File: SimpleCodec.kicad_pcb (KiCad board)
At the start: 4 copper layers, 59 x 95 mm, 89 parts, among them J1 RPI_ADC, J2 RP_GPIO, U1 AMS1117-5.0, U2 AMS1117-3.3, U3 MCP6002-xSN, U4 MCP6002-xSN, U5 CS4272, X1 PEDAL_COMBO_TOP

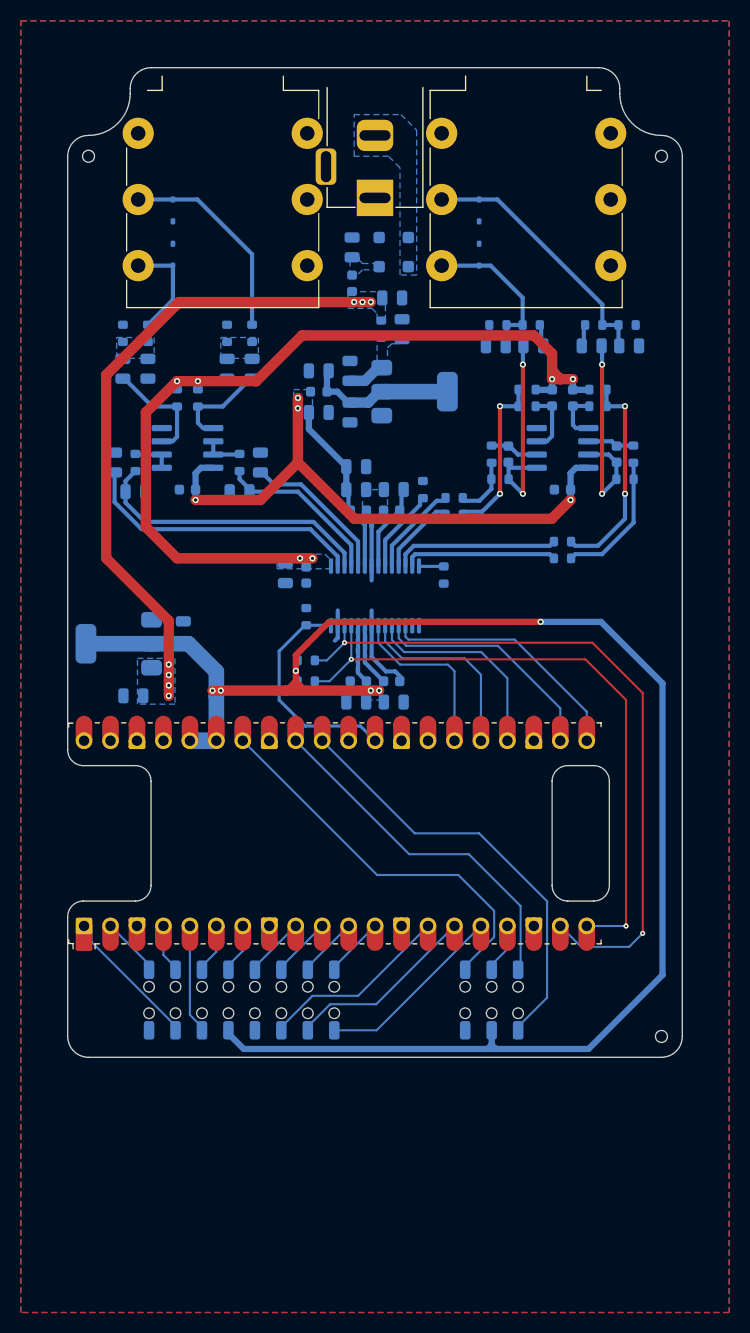
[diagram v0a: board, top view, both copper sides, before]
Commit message: Layout and power supply filtering
Updated the board layout.
Updated the project to KiCad 10.0.
Added additional power supply filtering.
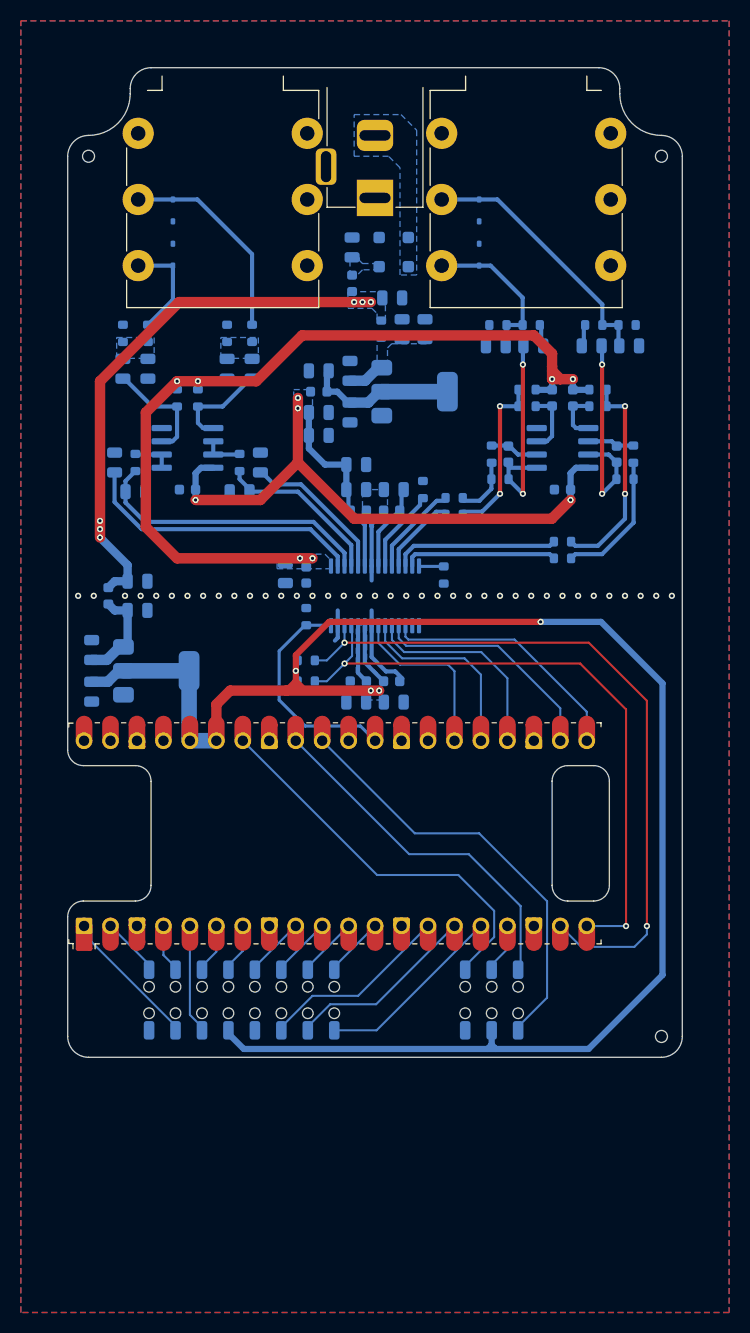
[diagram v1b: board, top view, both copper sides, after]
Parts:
- added C39: 10u, Capacitor_SMD:C_0805_2012Metric, B.Cu at (127.2, 91.8)
- added C40: 10u, Capacitor_SMD:C_0805_2012Metric, B.Cu at (127.2, 94.6)
- added C41: 10u, Capacitor_SMD:C_0805_2012Metric, B.Cu at (154.8, 67.6)
- added C42: 10u, Capacitor_SMD:C_0805_2012Metric, B.Cu at (148.2, 80.6)
- added FB3: 300, Inductor_SMD:L_0603_1608Metric, B.Cu at (124.4, 93.2)
- moved C10 10.5 mm to (122.8, 102.4), turned to -90 degrees
- moved C3 6.40 mm to (152.6, 67.6)
- moved C4 6.40 mm to (147.6, 71.6)
- moved C7 5.95 mm to (122.8, 98.4), turned to 90 degrees
- moved C9 4.69 mm to (144.6, 77.8)
- moved U2 4.44 mm to (129.0, 100.4), turned to 0 degrees
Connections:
- net +VCC_FILT renamed +VCC_FILTA
- C7 pad 1: +VCC -> +VCC_FILTD
- U2 pad 3: +VCC -> +VCC_FILTD
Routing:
- net +VCC_FILTD: track 0.00 -> 9.34 mm
- net +VCC: track 61.6 -> 53.9 mm, vias 7 -> 6
- net +5VA: track 72.3 -> 73.5 mm
- net +3V3D: track 172.8 -> 171.9 mm, vias 6 -> 4
- net GND: vias 0 -> 38
